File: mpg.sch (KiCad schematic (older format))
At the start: 39 parts, among them J1 Conn_01x04_Male, J2 DB25_Female_MountingHoles, J3 Conn_01x03_Male, J4 Screw_Terminal_01x02, J5 Screw_Terminal_01x03, J6 Screw_Terminal_01x03, K1 G5LE-1, Q1 BC847, Q2 BC847, Q3 BC847, Q4 BC847, Q5 BC847, SW1 SW_Push, U1 LD2981ABU33TR, U2 SP3485CN

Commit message: Corrected connectors.
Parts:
- removed J2: DB25_Female_MountingHoles, symbol Connector:DB25_Female_MountingHoles
- added J2: DB25_Male_MountingHoles, Connector_Dsub:DSUB-25_Male_Horizontal_P2.77x2.84mm_EdgePinOffset7.70mm_Housed_MountingHolesOffset9.12mm, symbol Connector:DB25_Male_MountingHoles
- D3, D4, D5: footprint (none) -> LED_THT:LED_D3.0mm
- D6: footprint (none) -> Diode_SMD:D_PowerDI-123
- J3: footprint (none) -> Connector_PinHeader_2.54mm:PinHeader_1x03_P2.54mm_Vertical
- J4: footprint (none) -> TerminalBlock_Phoenix:TerminalBlock_Phoenix_MPT-0,5-2-2.54_1x02_P2.54mm_Horizontal
- J5, J6: footprint (none) -> TerminalBlock_Phoenix:TerminalBlock_Phoenix_MPT-0,5-3-2.54_1x03_P2.54mm_Horizontal
- R1, R7, R8, R9: footprint (none) -> Resistor_SMD:R_0603_1608Metric
- renumbered U2 to U3
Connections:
- wire segments 158 -> 156

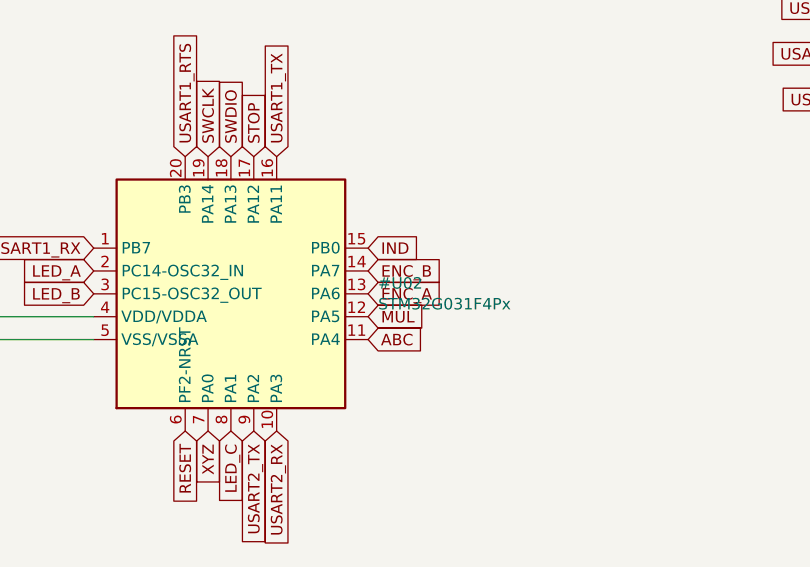
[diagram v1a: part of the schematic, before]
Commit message: Corrected STM32 symbol and generated PCB.
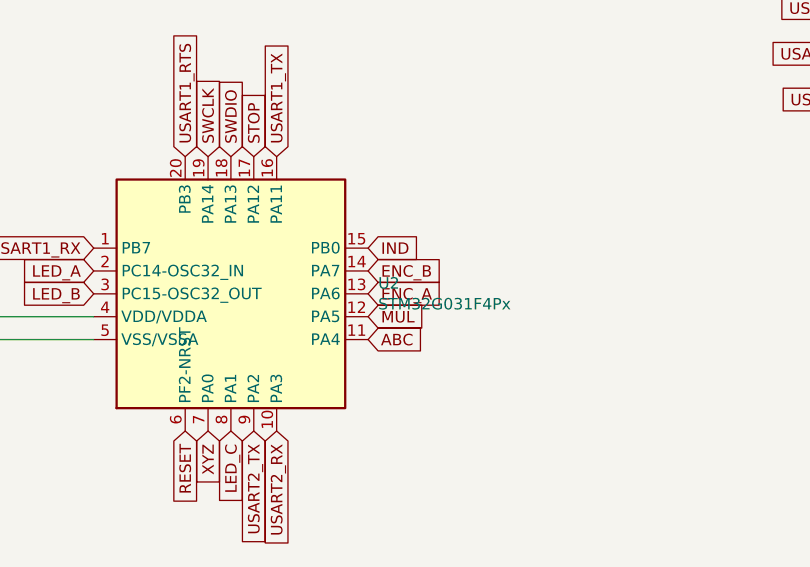
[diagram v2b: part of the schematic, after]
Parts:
- added U2: STM32G031F4Px, Package_SO:TSSOP-20_4.4x6.5mm_P0.65mm, symbol STM32G031F4Px:STM32G031F4Px
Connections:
- net +3V3: now also U2.4 (VDD/VDDA)
- net ABC: now also U2.11 (PA4)
- net ENC_A: now also U2.13 (PA6)
- net ENC_B: now also U2.14 (PA7)
- net GND: now also U2.5 (VSS/VSSA)
- net IND: now also U2.15 (PB0)
- net LED_A: now also U2.2 (PC14-OSC32_IN)
- net LED_B: now also U2.3 (PC15-OSC32_OUT)
- net LED_C: now also U2.8 (PA1)
- net MUL: now also U2.12 (PA5)
- net RESET: now also U2.6 (PF2-NRST)
- net STOP: now also U2.17 (PA12)
- net SWCLK: now also U2.19 (PA14)
- net SWDIO: now also U2.18 (PA13)
- net USART1_RTS: now also U2.20 (PB3)
- net USART1_RX: now also U2.1 (PB7)
- net USART1_TX: now also U2.16 (PA11)
- net USART2_RX: now also U2.10 (PA3)
- net USART2_TX: now also U2.9 (PA2)
- net XYZ: now also U2.7 (PA0)
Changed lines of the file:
@@
 Connection ~ 3000 2550
 $Comp
-L STM32G031F4Px:STM32G031F4Px #U02
-U 1 1 6068F881
+L STM32G031F4Px:STM32G031F4Px U2
+U 1 1 606BC4F3
 P 8450 4100
-F 0 "#U02" H 9094 4146 50  0000 L CNN
+F 0 "U2" H 9094 4146 50  0000 L CNN
 F 1 "STM32G031F4Px" H 9094 4055 50  0000 L CNN
-F 2 "" H 8450 4300 50  0001 C CNN
+F 2 "Package_SO:TSSOP-20_4.4x6.5mm_P0.65mm" H 8450 4300 50  0001 C CNN
 F 3 "" H 8450 4400 50  0001 C CNN
 	1    8450 4100

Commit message: Better layout.
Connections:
- net Sheet602C38D3/S1: now also J2.13; no longer J2.12
- net Sheet602C38D3/S2: now also J2.12; no longer J2.13
- net sheet603130A5/S1: now also J2.10; no longer J2.9
- net sheet603130A5/S2: now also J2.11; no longer J2.10
- net sheet603130A5/S3: now also J2.9; no longer J2.11
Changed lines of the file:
@@
 	3750 4850 3900 4850
 Wire Wire Line
-	2900 4750 3900 4750
-Wire Wire Line
 	2900 4550 3550 4550
-Wire Wire Line
-	3550 4550 3550 4650
-Wire Wire Line
-	3550 4650 3900 4650
 $Sheet
 S 3900 3950 550  400
@@
 $EndSheet
 Wire Wire Line
-	3550 4050 3900 4050
-Wire Wire Line
-	2900 4150 3900 4150
-Wire Wire Line
-	3550 4350 3550 4250
-Wire Wire Line
-	2900 4350 3550 4350
-Wire Wire Line
-	3550 4250 3900 4250
-Wire Wire Line
-	3550 3950 3550 4050
-Wire Wire Line
-	2900 3950 3550 3950
+	2900 4350 3500 4350
 $Sheet
 S 3900 5150 550  400
@@
 	1    0    0    -1
 $EndComp
+Wire Wire Line
+	3550 4750 3900 4750
+Wire Wire Line
+	3550 4550 3550 4750
+Wire Wire Line
+	2900 4750 3350 4750
+Wire Wire Line
+	3350 4750 3350 4650
+Wire Wire Line
+	3350 4650 3900 4650
+Wire Wire Line
+	3600 4250 3900 4250
+Wire Wire Line
+	2900 3950 3600 3950
+Wire Wire Line
+	2900 4150 3400 4150
+Wire Wire Line
+	3600 3950 3600 4250
+Wire Wire Line
+	3400 4050 3900 4050
+Wire Wire Line
+	3400 4050 3400 4150
+Wire Wire Line
+	3500 4150 3900 4150
+Wire Wire Line
+	3500 4150 3500 4350
 $EndSCHEMATC

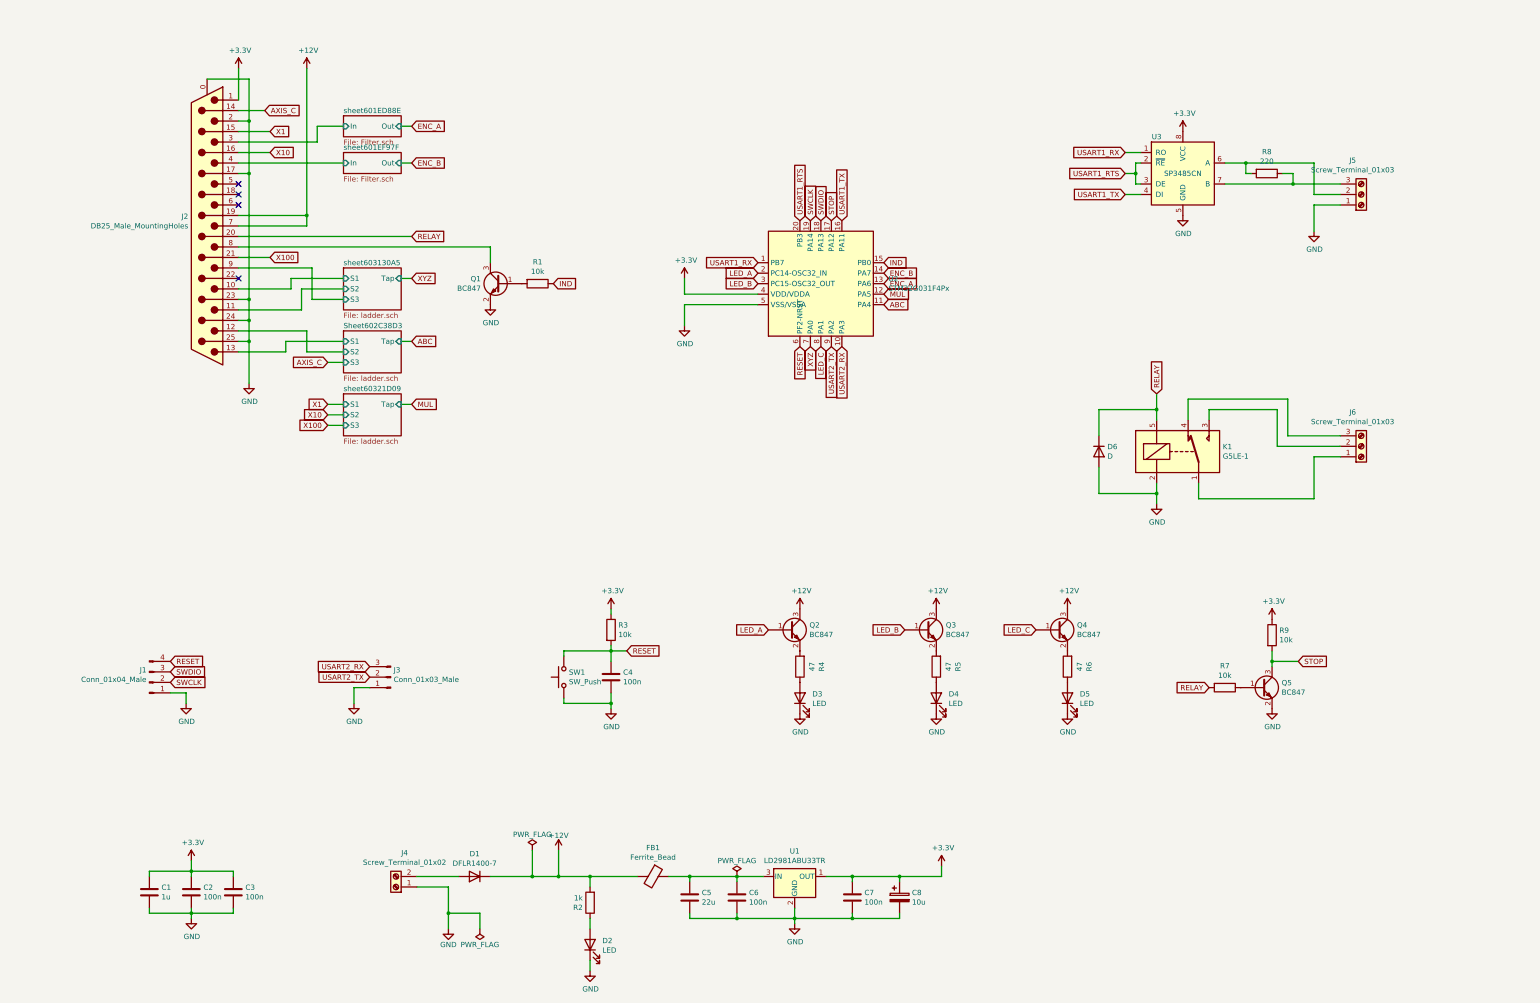
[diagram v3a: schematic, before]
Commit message: Use RJ45 connector.
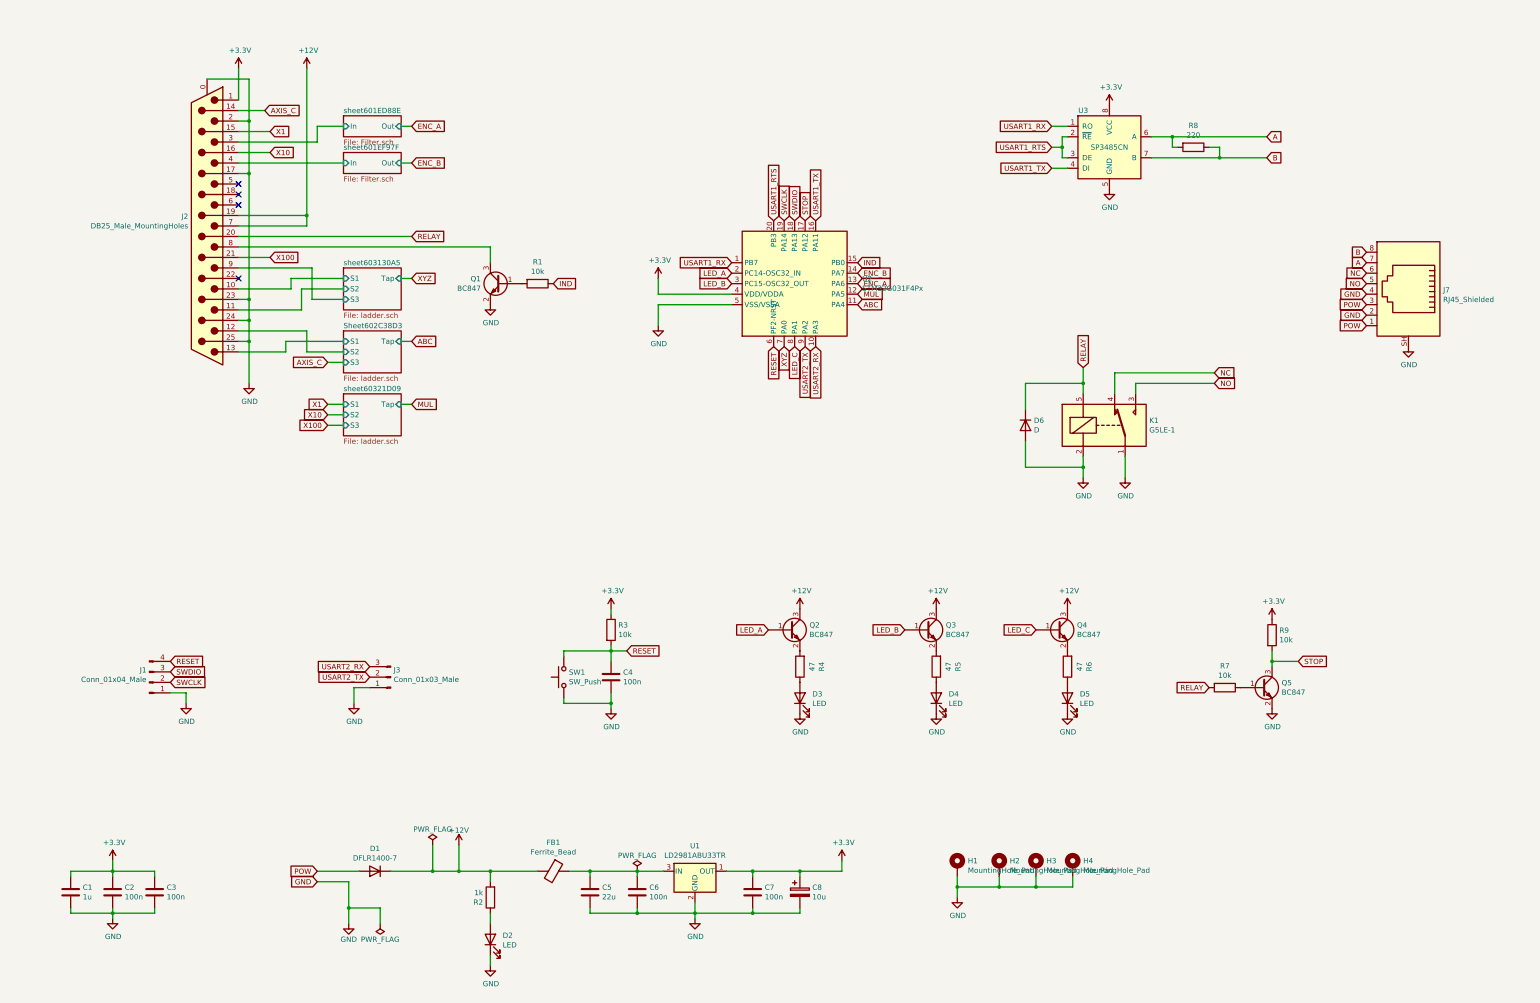
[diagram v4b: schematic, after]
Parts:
- removed J4: Screw_Terminal_01x02, TerminalBlock_Phoenix:TerminalBlock_Phoenix_MPT-0,5-2-2.54_1x02_P2.54mm_Horizontal, symbol Connector:Screw_Terminal_01x02
- removed J5, J6: Screw_Terminal_01x03, TerminalBlock_Phoenix:TerminalBlock_Phoenix_MPT-0,5-3-2.54_1x03_P2.54mm_Horizontal, symbol Connector:Screw_Terminal_01x03
- added H1, H2, H3, H4: MountingHole_Pad, MountingHole:MountingHole_3.2mm_M3_Pad_Via, symbol Mechanical:MountingHole_Pad
- added J7: RJ45_Shielded, Connector_RJ:RJ45_Amphenol_RJHSE5380, symbol Connector:RJ45_Shielded
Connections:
- net GND: now also K1.1, H1.1, H2.1, H3.1, H4.1, J7.2, J7.4, J7.SH
- net POW: now reaches D1.2 (A)
- net POW: now also J7.1, J7.3
- net A: now reaches R8.2, U3.6 (A)
- net A: now also J7.7
- net B: now reaches R8.1, U3.7 (B)
- net B: now also J7.8
- net NO: now reaches K1.3
- net NO: now also J7.5
- net NC: now reaches K1.4
- net NC: now also J7.6
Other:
- moved on the sheet: C1, C2, C3, C5, C6, C7, C8, D1, D2, D6, FB1, K1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

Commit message: Redesigned around G431.
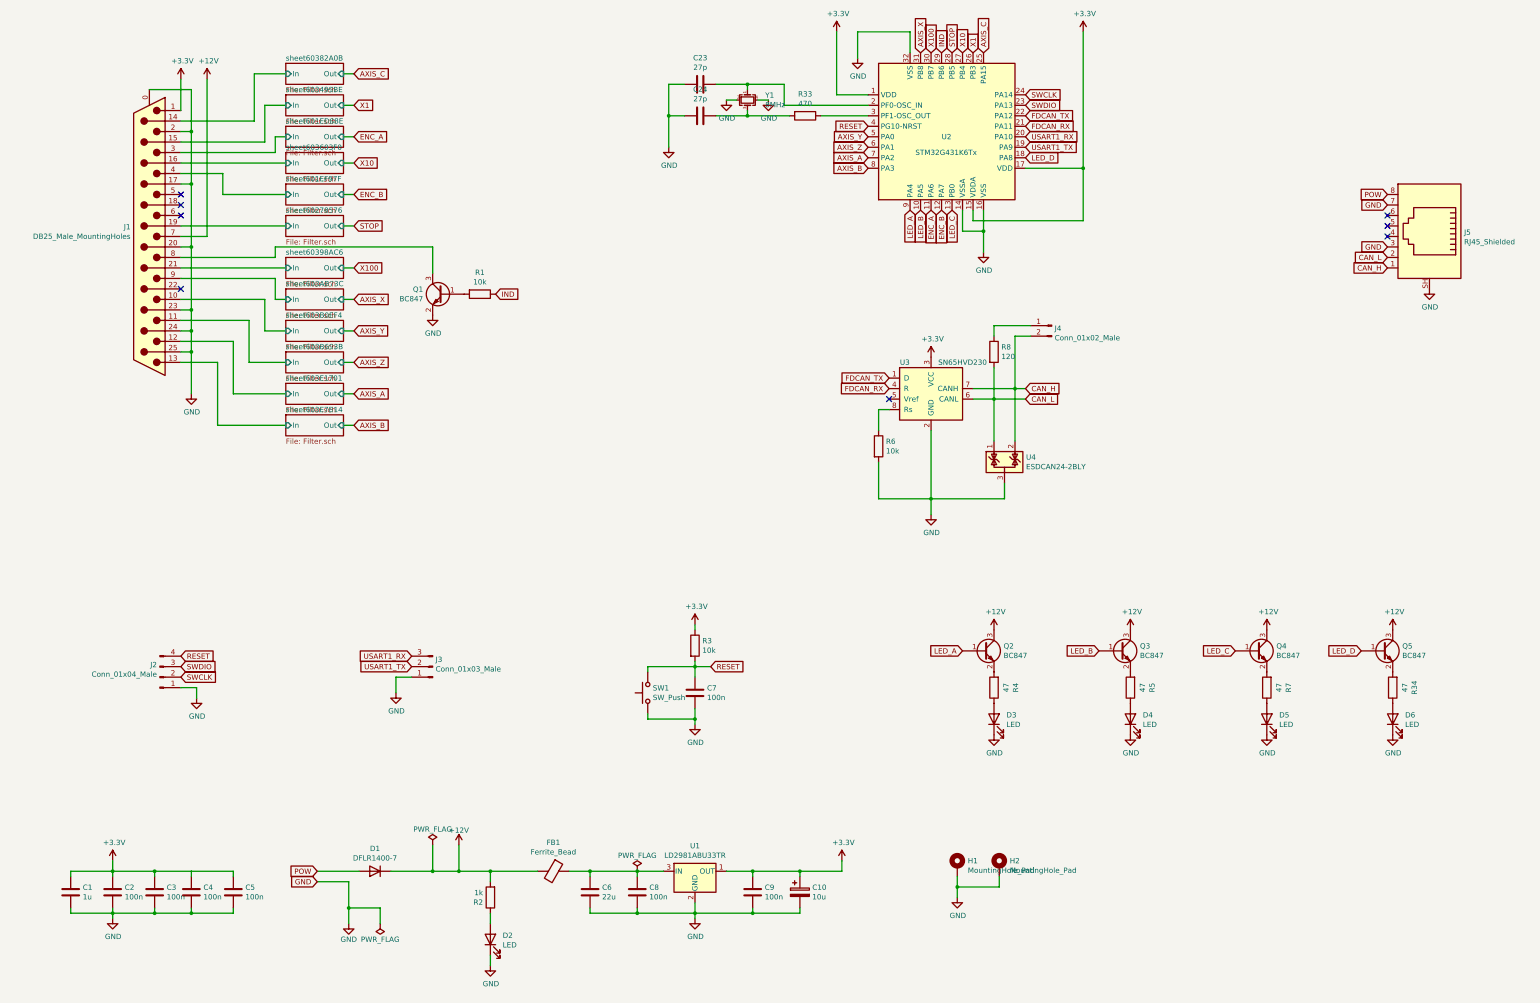
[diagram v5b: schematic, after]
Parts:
- removed D6: D, Diode_SMD:D_PowerDI-123, symbol Device:D
- removed H3, H4: MountingHole_Pad, MountingHole:MountingHole_3.2mm_M3_Pad_Via, symbol Mechanical:MountingHole_Pad
- removed K1: G5LE-1, Relay_THT:Relay_SPDT_Omron-G5LE-1, symbol Relay:G5LE-1
- removed R7, R9: 10k, Resistor_SMD:R_0603_1608Metric, symbol Device:R
- removed U2: STM32G031F4Px, Package_SO:TSSOP-20_4.4x6.5mm_P0.65mm, symbol STM32G031F4Px:STM32G031F4Px
- removed U3: SP3485CN, Package_SO:SOIC-8_3.9x4.9mm_P1.27mm, symbol Interface_UART:SP3485CN
- added C23, C24: 27p, Capacitor_SMD:C_0603_1608Metric, symbol Device:C
- added C4, C5: 100n, Capacitor_SMD:C_0603_1608Metric, symbol Device:C
- added D6: LED, LED_THT:LED_D3.0mm, symbol Device:LED
- added J4: Conn_01x02_Male, Connector_PinHeader_2.54mm:PinHeader_1x01_P2.54mm_Vertical, symbol Connector:Conn_01x02_Male
- added R33: 470, Resistor_SMD:R_0603_1608Metric, symbol Device:R
- added R34: 47, Resistor_SMD:R_0603_1608Metric, symbol Device:R
- added R6: 10k, Resistor_SMD:R_0603_1608Metric, symbol Device:R
- added U2: STM32G431K6Tx, Package_QFP:LQFP-32_7x7mm_P0.8mm, symbol STM32G431K6Tx:STM32G431K6Tx
- added U3: SN65HVD230, Package_SO:SOIC-8_3.9x4.9mm_P1.27mm, symbol Interface_CAN_LIN:SN65HVD230
- added U4: ESDCAN24-2BLY, Package_TO_SOT_SMD:SOT-23, symbol Power_Protection:NUP2105L
- added Y1: 8MHz, Crystal:Crystal_SMD_5032-4Pin_5.0x3.2mm, symbol Device:Crystal_GND24_Small
- R8: value 220 -> 120
- renumbered C8 to C10, C5 to C6, C4 to C7, C6 to C8, C7 to C9, J2 to J1, J1 to J2, J7 to J5, R6 to R7
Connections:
- net RELAY is gone; now on net GND: J1.20 (P20)
- net USART2_RX is gone; now on net USART1_RX: J3.3 (Pin_3)
- net USART2_TX is gone; now on net USART1_TX: J3.2 (Pin_2)
- net +12V: now also Q5.3 (C); no longer J1.19 (P19)
- net +3V3: now also C4.1, C5.1, U2.1 (VDD), U2.15 (VDDA), U2.17 (VDD), U3.3 (VCC)
- net AXIS_C: now also U2.25 (PA15); no longer J1.14 (P14)
- net ENC_A: now also U2.11 (PA6)
- net ENC_B: now also U2.12 (PA7)
- net GND: now also J5.3, J5.7, C23.2, C24.2, C4.2, C5.2, D6.1 (K), R6.2, U2.14 (VSSA), U2.16 (VSS), U2.32 (VSS), U3.2 (GND), U4.3 (A), Y1.2, Y1.4; no longer J5.2, J5.4, Q5.2 (E)
- net IND: now also U2.29 (PB6)
- net LED_A: now also U2.9 (PA4)
- net LED_B: now also U2.10 (PA5)
- net LED_C: now also U2.13 (PB0)
- net POW: now also J5.8; no longer J5.1, J5.3
- net RESET: now also U2.4 (PG10-NRST)
- net STOP: now also U2.28 (PB5); no longer Q5.3 (C)
- net SWCLK: now also U2.24 (PA14)
- net SWDIO: now also U2.23 (PA13)
- net USART1_RX: now also U2.20 (PA10)
- net USART1_TX: now also U2.19 (PA9)
- net X1: now also U2.26 (PB3); no longer J1.15 (P15)
- net X10: now also U2.27 (PB4); no longer J1.16 (P16)
- net X100: now also U2.30 (PB7); no longer J1.21 (P21)
- net LED_D: now reaches Q5.1 (B)
- net LED_D: now also U2.18 (PA8)
- net A renamed CAN_L
- net CAN_L: now also J5.2, U3.6 (CANL), U4.1 (K); no longer J5.7
- net B: no longer names the net of R8.1
- net B: now also J4.1 (Pin_1); no longer J5.8
- net NC: no longer names the net of J5.6
- net NO: no longer names the net of J5.5
- net Sheet602C38D3/S1 renamed sheet603E7B14/In
- net Sheet602C38D3/S2 renamed sheet603E1701/In
- net sheet603130A5/S1 renamed sheet603B0EF4/In
- net sheet603130A5/S2 renamed sheet603B693B/In
- net sheet603130A5/S3 renamed sheet603AB73C/In
- new net: R6.1, U3.8 (Rs)
- new net: C23.1, U2.2 (PF0-OSC_IN), Y1.1
- new net: R33.1, U2.3 (PF1-OSC_OUT)
- new net: D6.2 (A), R34.1
- new net: Q5.2 (E), R34.2
- new net: C24.1, R33.2, Y1.3
- new net AXIS_A: U2.7 (PA2)
- new net AXIS_B: U2.8 (PA3)
- new net AXIS_X: U2.31 (PB8)
- new net AXIS_Y: U2.5 (PA0)
- new net AXIS_Z: U2.6 (PA1)
- new net CAN_H: J4.2 (Pin_2), J5.1, U3.7 (CANH), U4.2 (K)
- new net FDCAN_RX: U2.21 (PA11), U3.4 (R)
- new net FDCAN_TX: U2.22 (PA12), U3.1 (D)
- new net sheet60278576/In: J1.19 (P19)
- new net sheet603499BE/In: J1.15 (P15)
- new net sheet603603F0/In: J1.16 (P16)
- new net sheet60382A0B/In: J1.14 (P14)
- new net sheet60398AC6/In: J1.21 (P21)
- no-connect marks 4 -> 8
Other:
- moved on the sheet: C7, D3, D4, D5, J1, J2, J3, J5, Q1, Q2, Q3, Q4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
